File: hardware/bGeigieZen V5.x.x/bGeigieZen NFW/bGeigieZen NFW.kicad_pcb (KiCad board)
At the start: 2 copper layers, 129.4 x 64.6 mm, 13 parts, among them J1 M5 2x15 pin, J3 GPS, J4 Geiger Safepulse, J5 Extra support header

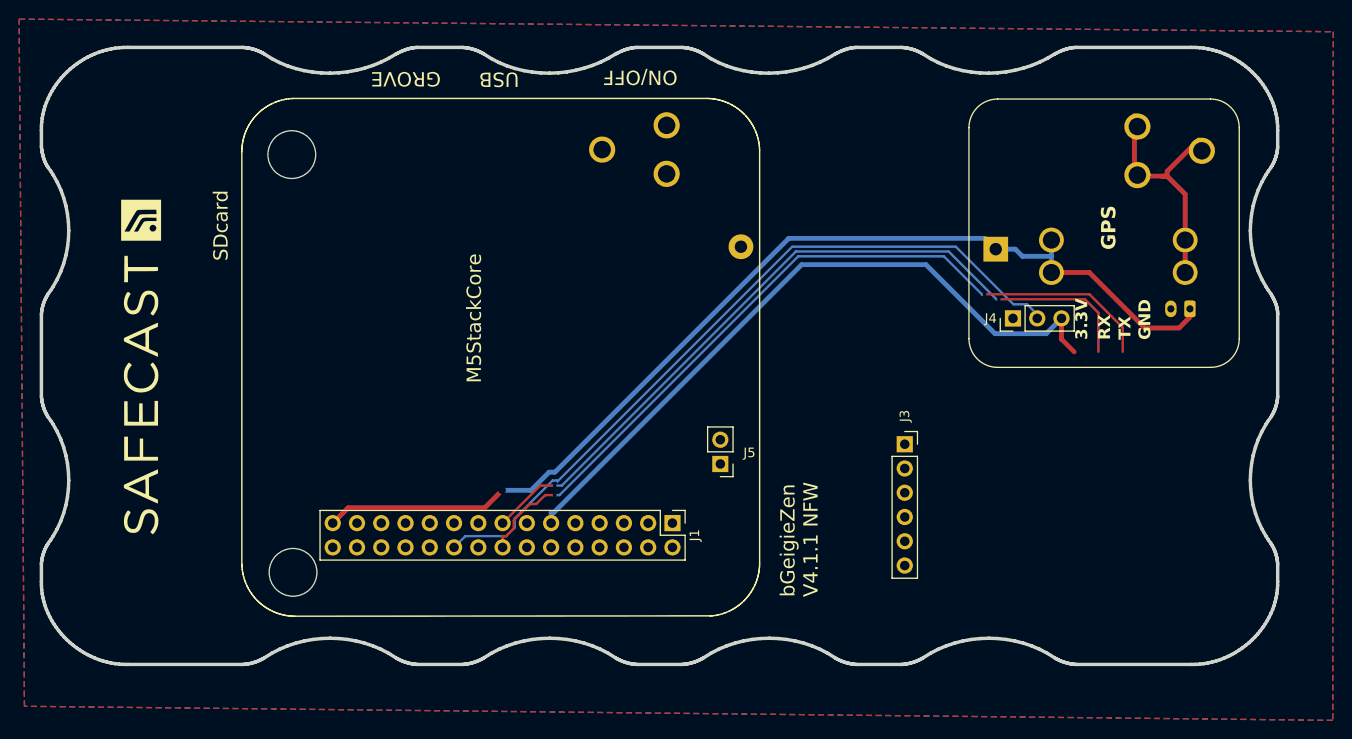
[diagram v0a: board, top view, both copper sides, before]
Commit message: Update V4.2.0 boards and V5.x.x. boards
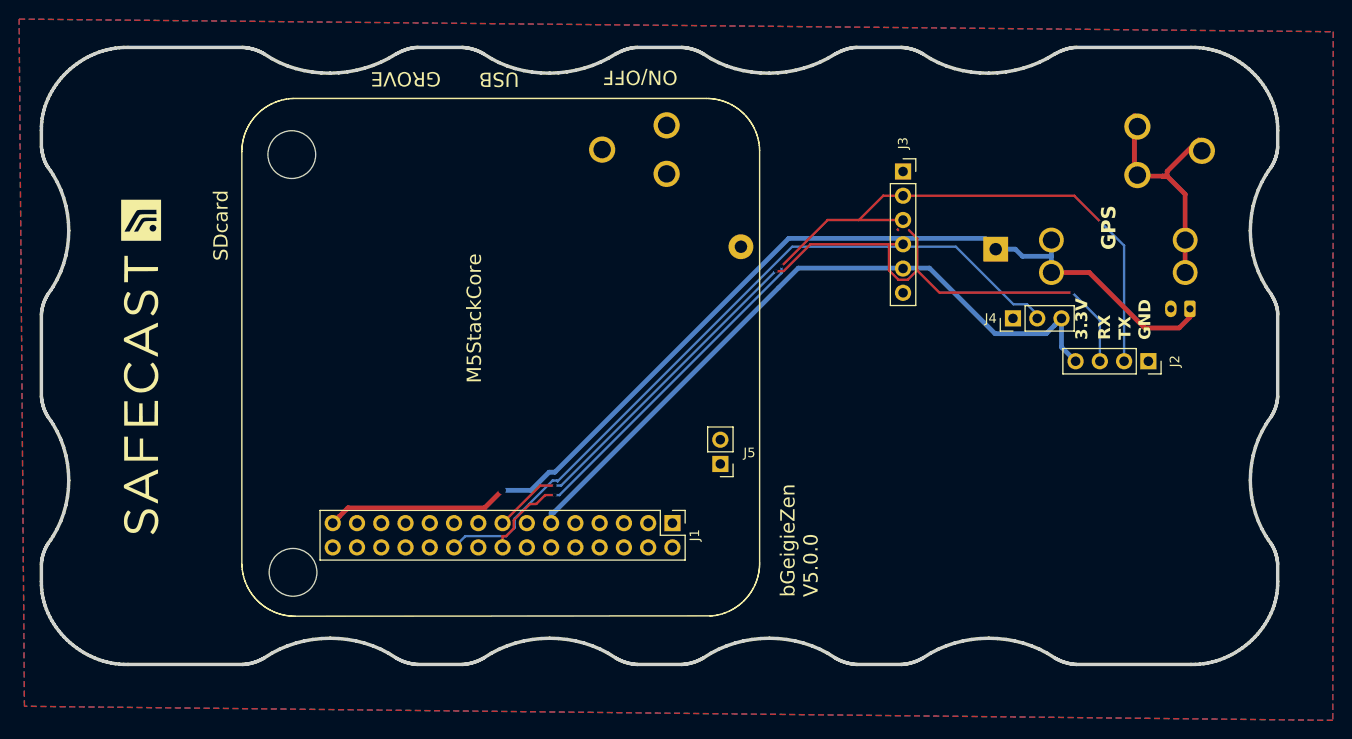
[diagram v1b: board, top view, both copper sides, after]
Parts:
- added J2: GPS, Connector_PinSocket_2.54mm:PinSocket_1x04_P2.54mm_Vertical, F.Cu at (200.5, 99.5)
- J3: value GPS -> Notecard
- moved J3 28.6 mm to (174.8, 79.7)
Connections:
- BT1 pad 1: GND -> Net-(BT1-+)
- BT1 pad PWR@2: GND -> (no net)
- BT1 pad PWR@3: GND -> (no net)
- J3 pad 1: unconnected-(J3-Pin_1-Pad1) -> GND
- J3 pad 2: GND -> /TX2
- J3 pad 3: /TX2 -> /RX2
- J3 pad 4: /RX2 -> 3.3V
- J3 pad 5: 3.3V -> (no net)
- J3 pad 6: unconnected-(J3-Pin_6-Pad6) -> (no net)
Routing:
- net /TX2: track 84.4 -> 101.4 mm, vias 2 -> 3
- net /RX2: track 80.9 -> 91.9 mm, vias 2 -> 3
- net /BAT: track 110.0 -> 112.9 mm
- net 3.3V: track 73.0 -> 74.7 mm
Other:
- board text added: "bGeigieZen V5.0.0"
- board text removed: "bGeigieZen V4.1.1 NFW"
